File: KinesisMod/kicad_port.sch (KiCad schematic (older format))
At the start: 15 parts, among them J1 Conn_01x13, J2 Conn_01x13, J3 Conn_01x13, J4 Conn_01x13, J5 Conn_01x10, J6 Conn_01x10, U1 Teensy++_2_0

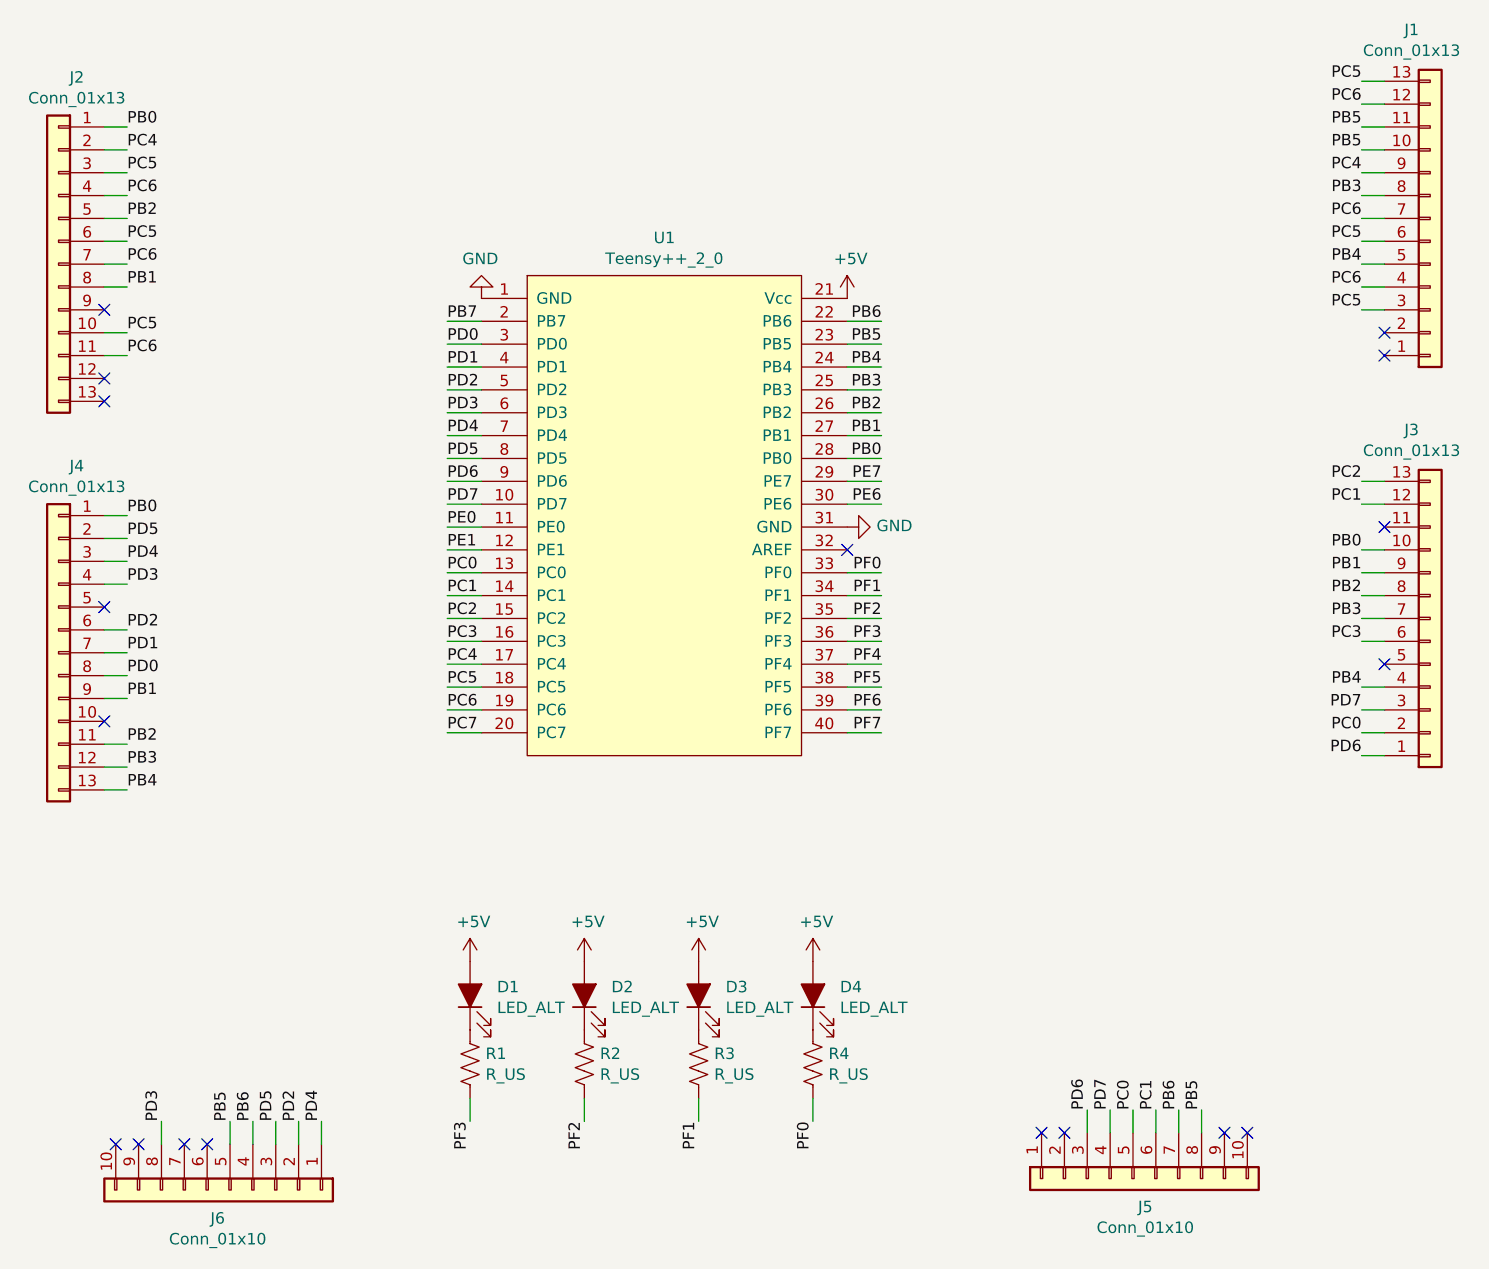
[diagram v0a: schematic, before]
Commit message: parts were not on correct side of board, had to re-orient and re-route. In addition I added the 3d Models for the other parts
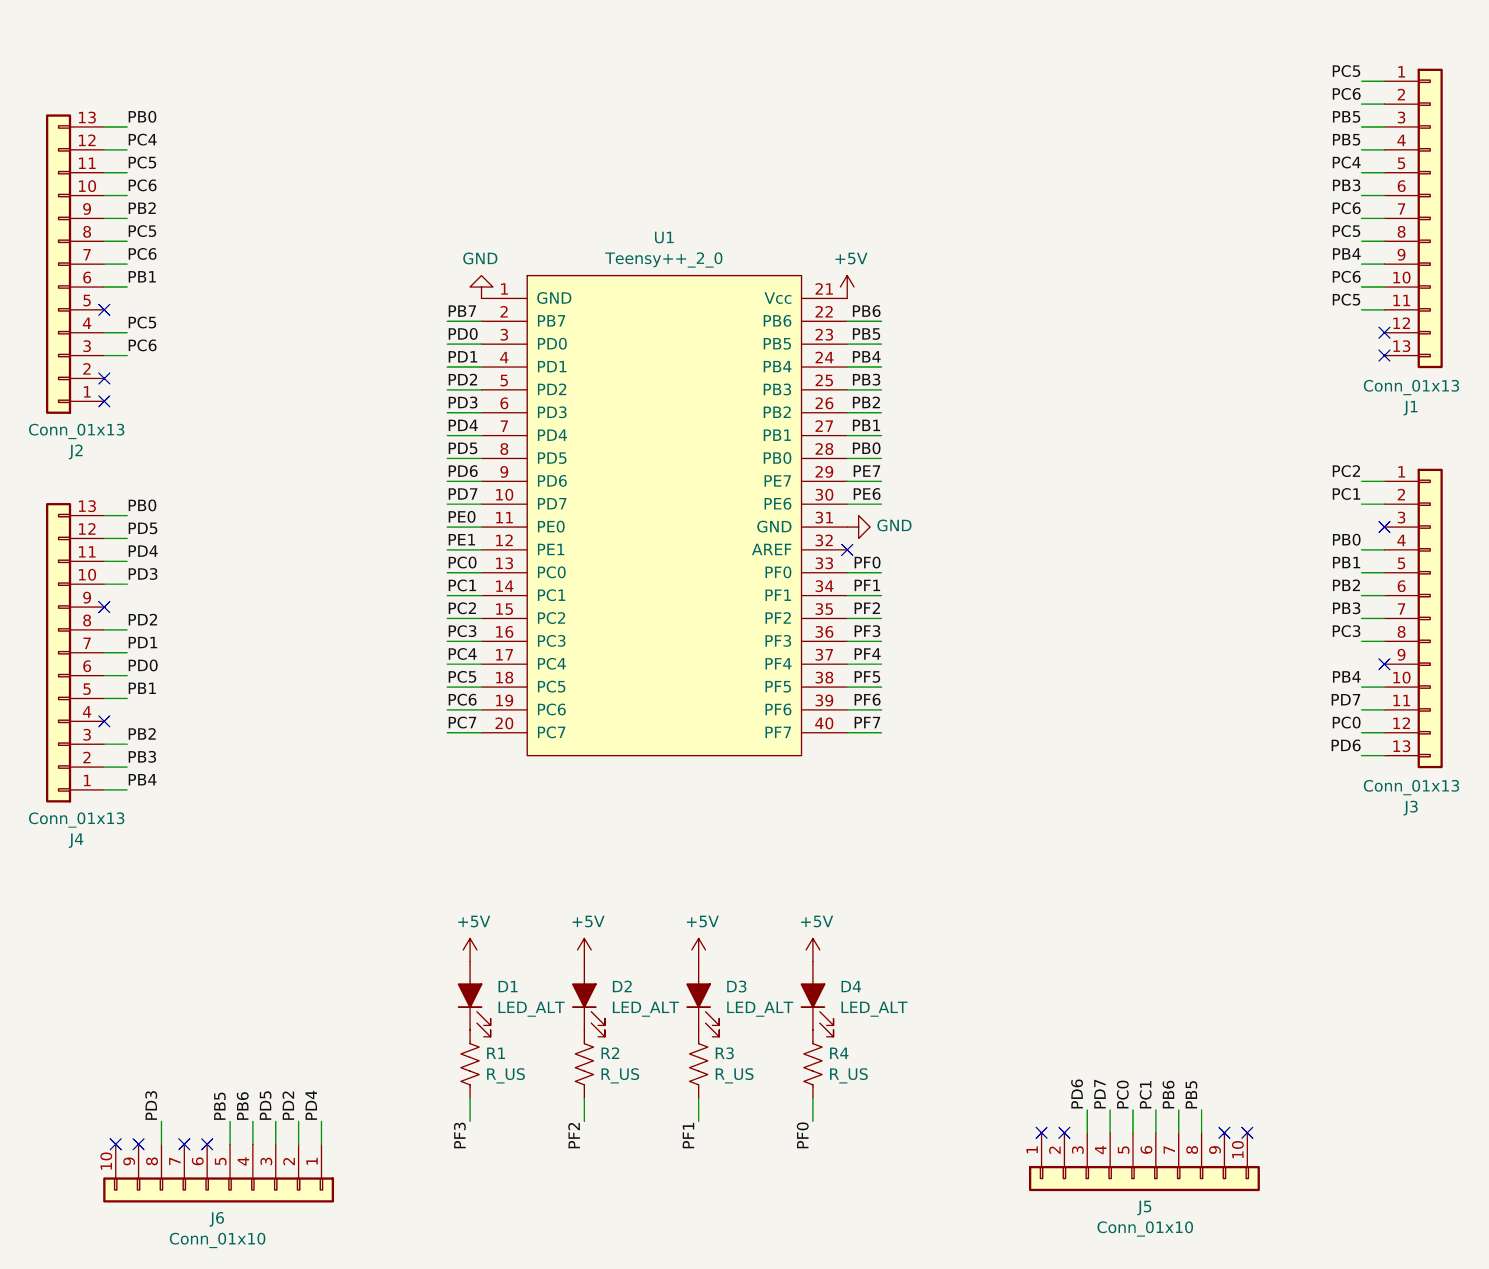
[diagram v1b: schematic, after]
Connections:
- net PB0: now also J2.13 (Pin_13), J3.4 (Pin_4), J4.13 (Pin_13); no longer J2.1 (Pin_1), J3.10 (Pin_10), J4.1 (Pin_1)
- net PB1: now also J2.6 (Pin_6), J3.5 (Pin_5), J4.5 (Pin_5); no longer J2.8 (Pin_8), J3.9 (Pin_9), J4.9 (Pin_9)
- net PB2: now also J2.9 (Pin_9), J3.6 (Pin_6), J4.3 (Pin_3); no longer J2.5 (Pin_5), J3.8 (Pin_8), J4.11 (Pin_11)
- net PB3: now also J1.6 (Pin_6), J4.2 (Pin_2); no longer J1.8 (Pin_8), J4.12 (Pin_12)
- net PB4: now also J1.9 (Pin_9), J3.10 (Pin_10), J4.1 (Pin_1); no longer J1.5 (Pin_5), J3.4 (Pin_4), J4.13 (Pin_13)
- net PB5: now also J1.3 (Pin_3), J1.4 (Pin_4); no longer J1.10 (Pin_10), J1.11 (Pin_11)
- net PC0: now also J3.12 (Pin_12); no longer J3.2 (Pin_2)
- net PC1: now also J3.2 (Pin_2); no longer J3.12 (Pin_12)
- net PC2: now also J3.1 (Pin_1); no longer J3.13 (Pin_13)
- net PC3: now also J3.8 (Pin_8); no longer J3.6 (Pin_6)
- net PC4: now also J1.5 (Pin_5), J2.12 (Pin_12); no longer J1.9 (Pin_9), J2.2 (Pin_2)
- net PC5: now also J1.1 (Pin_1), J1.11 (Pin_11), J1.8 (Pin_8), J2.11 (Pin_11), J2.4 (Pin_4), J2.8 (Pin_8); no longer J1.13 (Pin_13), J1.3 (Pin_3), J1.6 (Pin_6), J2.10 (Pin_10), J2.3 (Pin_3), J2.6 (Pin_6)
- net PC6: now also J1.10 (Pin_10), J1.2 (Pin_2), J2.10 (Pin_10), J2.3 (Pin_3); no longer J1.12 (Pin_12), J1.4 (Pin_4), J2.11 (Pin_11), J2.4 (Pin_4)
- net PD0: now also J4.6 (Pin_6); no longer J4.8 (Pin_8)
- net PD2: now also J4.8 (Pin_8); no longer J4.6 (Pin_6)
- net PD3: now also J4.10 (Pin_10); no longer J4.4 (Pin_4)
- net PD4: now also J4.11 (Pin_11); no longer J4.3 (Pin_3)
- net PD5: now also J4.12 (Pin_12); no longer J4.2 (Pin_2)
- net PD6: now also J3.13 (Pin_13); no longer J3.1 (Pin_1)
- net PD7: now also J3.11 (Pin_11); no longer J3.3 (Pin_3)
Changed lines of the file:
@@
 F 3 "~" H 2450 3400 50  0001 C CNN
 	1    2450 3400
-	-1   0    0    -1
+	-1   0    0    1
 $EndComp
 $Comp
@@
 F 3 "~" H 8450 3250 50  0001 C CNN
 	1    8450 3250
-	1    0    0    1
+	1    0    0    -1
 $EndComp
 $Comp
@@
 F 3 "~" H 2450 1700 50  0001 C CNN
 	1    2450 1700
-	-1   0    0    -1
+	-1   0    0    1
 $EndComp
 $Comp
@@
 F 3 "~" H 8450 1500 50  0001 C CNN
 	1    8450 1500
-	1    0    0    1
+	1    0    0    -1
 $EndComp
 $Comp
